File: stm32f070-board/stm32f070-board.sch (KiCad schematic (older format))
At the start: 39 parts, among them J1 USB_B_Micro, J2 USB_B_Micro, J3 Conn_01x05_Male, SW1 SW_DPDT_x2, SW2 SW_Push, SW3 SW_Push, U1 CH340G, U2 STM32F070F6P6, U3 MCP9700AT-ETT, U4 Si7055-A20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

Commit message: added mechanical drawing from ch340g soic16 and updated footprints for stm32 in schematic
Signed-off-by: suyash <in.suyash@gmail.com>
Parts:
- J3: footprint (none) -> Connector_PinHeader_1.00mm:PinHeader_1x05_P1.00mm_Vertical
- U2: footprint (none) -> stm32f070-board:TSSOP20_P0.65mm
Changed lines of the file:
@@
 F 0 "U2" H 6200 550 50  0000 C CNN
 F 1 "STM32F070F6P6" H 5850 1850 50  0000 C CNN
-F 2 "" H 5800 2000 50  0001 C CNN
+F 2 "stm32f070-board:TSSOP20_P0.65mm" H 5800 2000 50  0001 C CNN
 F 3 "http://www.farnell.com/datasheets/2281751.pdf" H 5800 2000 50  0001 C CNN
 F 4 "https://in.element14.com/stmicroelectronics/stm32f070f6p6tr/mcu-32bit-48mhz-tssop-20/dp/3129808?ost=3129808&ddkey=https%3Aen-IN%2FElement14_India%2Fsearch" H 5950 2200 50  0001 C CNN "Vendor"
@@
 F 0 "J3" H 9800 2550 50  0000 C CNN
 F 1 "Conn_01x05_Male" H 9800 2400 50  0000 C CNN
-F 2 "" H 9600 2050 50  0001 C CNN
+F 2 "Connector_PinHeader_1.00mm:PinHeader_1x05_P1.00mm_Vertical" H 9600 2050 50  0001 C CNN
 F 3 "http://www.farnell.com/datasheets/2368223.pdf" H 9600 2050 50  0001 C CNN
 F 4 "https://in.element14.com/harwin/m52-040023v0545/header-tht-vertical-1-27mm-5way/dp/1099560" H 0   0   50  0001 C CNN "Vendor"

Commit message: changed the vendor of tactile user switch from robu to element14
Signed-off-by: suyash <in.suyash@gmail.com>
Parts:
- SW2, SW3: Vendor https://robu.in/product/362-5mm-tactile-push-button-switch-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 -> https://in.element14.com/alcoswitch-te-connectivity/fsmsm/s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
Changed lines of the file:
@@
 F 1 "SW_Push" H 3850 1294 50  0000 C CNN
 F 2 "" H 3850 1300 50  0001 C CNN
-F 3 "" H 3850 1300 50  0001 C CNN
-F 4 "https://robu.in/product/362-5mm-tactile-push-button-switch-20pcs/" H 3850 1100 50  0001 C CNN "Vendor"
+F 3 "http://www.farnell.com/datasheets/1754085.pdf" H 3850 1300 50  0001 C CNN
+F 4 "https://in.element14.com/alcoswitch-te-connectivity/fsmsm/switch-spst-0-05a-24vdc-smd/dp/1703878" H 3850 1100 50  0001 C CNN "Vendor"
 	1    3850 1100
 	1    0    0    -1
@@
 F 1 "SW_Push" H 7350 1494 50  0000 C CNN
 F 2 "" H 7350 1500 50  0001 C CNN
-F 3 "" H 7350 1500 50  0001 C CNN
-F 4 "https://robu.in/product/362-5mm-tactile-push-button-switch-20pcs/" H 7350 1300 50  0001 C CNN "Vendor"
+F 3 "http://www.farnell.com/datasheets/1754085.pdf" H 7350 1500 50  0001 C CNN
+F 4 "https://in.element14.com/alcoswitch-te-connectivity/fsmsm/switch-spst-0-05a-24vdc-smd/dp/1703878" H 7350 1300 50  0001 C CNN "Vendor"
 	1    7350 1300
 	1    0    0    -1

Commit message: created footprint for tactile switch and updated it in the schematic
Signed-off-by: suyash <in.suyash@gmail.com>
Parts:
- SW2, SW3: footprint (none) -> stm32f070-board:TACTILE_SWITCH_3.5X6.0mm
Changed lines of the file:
@@
 F 0 "SW2" H 3850 1385 50  0000 C CNN
 F 1 "SW_Push" H 3850 1294 50  0000 C CNN
-F 2 "" H 3850 1300 50  0001 C CNN
+F 2 "stm32f070-board:TACTILE_SWITCH_3.5X6.0mm" H 3850 1300 50  0001 C CNN
 F 3 "http://www.farnell.com/datasheets/1754085.pdf" H 3850 1300 50  0001 C CNN
 F 4 "https://in.element14.com/alcoswitch-te-connectivity/fsmsm/switch-spst-0-05a-24vdc-smd/dp/1703878" H 3850 1100 50  0001 C CNN "Vendor"
@@
 F 0 "SW3" H 7350 1585 50  0000 C CNN
 F 1 "SW_Push" H 7350 1494 50  0000 C CNN
-F 2 "" H 7350 1500 50  0001 C CNN
+F 2 "stm32f070-board:TACTILE_SWITCH_3.5X6.0mm" H 7350 1500 50  0001 C CNN
 F 3 "http://www.farnell.com/datasheets/1754085.pdf" H 7350 1500 50  0001 C CNN
 F 4 "https://in.element14.com/alcoswitch-te-connectivity/fsmsm/switch-spst-0-05a-24vdc-smd/dp/1703878" H 7350 1300 50  0001 C CNN "Vendor"

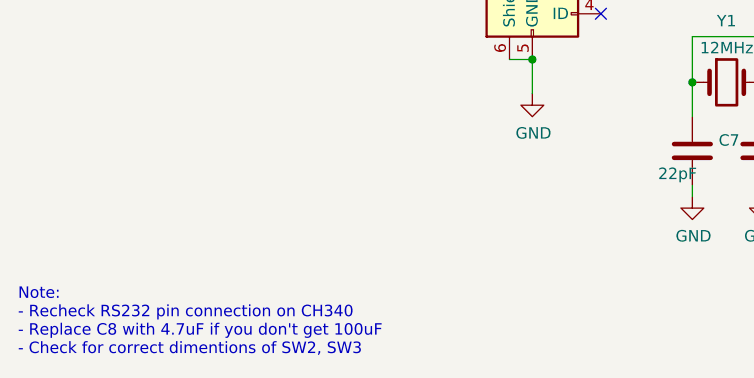
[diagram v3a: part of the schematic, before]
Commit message: created footprint for the slide switch and updated the same in schematic
Signed-off-by: suyash <in.suyash@gmail.com>
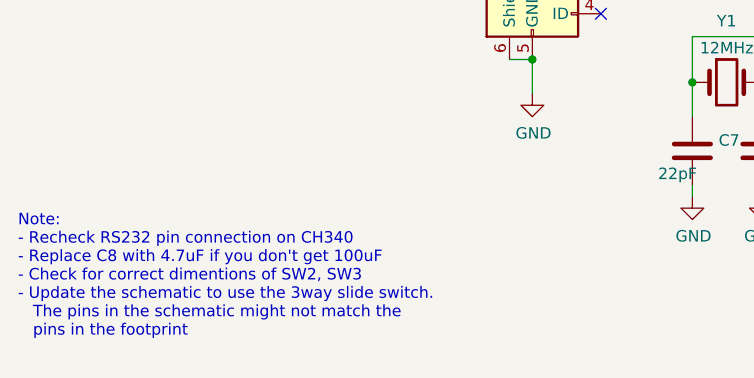
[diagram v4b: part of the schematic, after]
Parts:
- SW1: footprint (none) -> stm32f070-board:SLIDE_SWITCH_3.6x9.0mm
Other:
- note added: "Note: \n- Recheck RS232 pin connection on CH340\n- Replace C8 with 4.7uF if you don't get 100uF\n- Check for correct dimentions of SW2, SW3\n- Update the schematic to use the 3way slide switch.\n The pins in the schematic might not match the \n pins in the footprint\n\n"
- note removed: "Note: \n- Recheck RS232 pin connection on CH340\n- Replace C8 with 4.7uF if you don't get 100uF\n- Check for correct dimentions of SW2, SW3\n"
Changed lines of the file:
@@
 F 0 "SW1" H 3600 2385 50  0000 C CNN
 F 1 "SW_DPDT_x2" H 3500 2300 50  0000 C CNN
-F 2 "" H 3600 2100 50  0001 C CNN
+F 2 "stm32f070-board:SLIDE_SWITCH_3.6x9.0mm" H 3600 2100 50  0001 C CNN
 F 3 "http://www.farnell.com/datasheets/2674788.pdf" H 3600 2100 50  0001 C CNN
 F 4 "https://in.element14.com/c-k-components/js202011jcqn/slide-switch-dpdt-0-3a-6vdc-smd/dp/2931766" H 3600 2100 50  0001 C CNN "Vendor"
@@
 	7150 1300 7050 1300
 Text Notes 600  7250 0    50   ~ 0
-Note: \n- Recheck RS232 pin connection on CH340\n- Replace C8 with 4.7uF if you don't get 100uF\n- Check for correct dimentions of SW2, SW3\n
+Note: \n- Recheck RS232 pin connection on CH340\n- Replace C8 with 4.7uF if you don't get 100uF\n- Check for correct dimentions of SW2, SW3\n- Update the schematic to use the 3way slide switch.\n   The pins in the schematic might not match the \n   pins in the footprint\n\n
 Connection ~ 3800 3250
 Wire Wire Line

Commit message: added footprint for rgb led in schematic
Signed-off-by: suyash <in.suyash@gmail.com>
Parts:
- D3: footprint (none) -> stm32f070-board:PLCC6
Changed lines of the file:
@@
 F 0 "D3" H 7100 2283 50  0000 C CNN
 F 1 "LED_RGB" H 7100 2374 50  0000 C CNN
-F 2 "" H 7100 2700 50  0001 C CNN
+F 2 "stm32f070-board:PLCC6" H 7100 2700 50  0001 C CNN
 F 3 "http://www.farnell.com/datasheets/2573293.pdf" H 7100 2700 50  0001 C CNN
 F 4 "https://in.element14.com/cree/clx6f-fkc-cnp1st1e1bb7d3d3/led-aec-q101-rgb-750-1350-240mcd/dp/2840590?st=rgb%20led" H 7100 2750 50  0001 C CNN "Vendor"

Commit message: added footprint for voltage regulator and updated schematic
Signed-off-by: suyash <in.suyash@gmail.com>
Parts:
- VR1: footprint (none) -> LD39050PU33R:SON95P300X300X100-7N
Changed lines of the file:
@@
 F 0 "VR1" H 2950 3820 50  0000 C CNN
 F 1 "LD39050PU33R" H 2950 3729 50  0000 C CNN
-F 2 "" H 2950 3450 50  0001 C CNN
+F 2 "LD39050PU33R:SON95P300X300X100-7N" H 2950 3450 50  0001 C CNN
 F 3 "http://www.farnell.com/datasheets/2370074.pdf" H 2950 3450 50  0001 C CNN
 F 4 "https://in.element14.com/stmicroelectronics/ld39050pu33r/ldo-fixed-3-3v-0-5a-dfn-6/dp/2762703" H 2950 3400 50  0001 C CNN "Vendor"

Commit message: added footprint for the crystal and updated it in the schematic
Signed-off-by: suyash <in.suyash@gmail.com>
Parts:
- Y1: footprint (none) -> stm32f070-board:HC_49US-(AT49)_1
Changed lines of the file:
@@
 F 0 "Y1" H 3700 6318 50  0000 C CNN
 F 1 "12MHz" H 3700 6200 50  0000 C CNN
-F 2 "" H 3700 6050 50  0001 C CNN
+F 2 "stm32f070-board:HC_49US-(AT49)_1" H 3700 6050 50  0001 C CNN
 F 3 "http://www.farnell.com/datasheets/1883669.pdf" H 3700 6050 50  0001 C CNN
 F 4 "https://in.element14.com/abracon/abls-12-000mhz-b4-t/crystal-12mhz-18pf-hc-49us/dp/2467716" H 3700 6050 50  0001 C CNN "Vendor"

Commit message: added footprint for usb cable from mouser.in and added in schematic
Signed-off-by: suyash <in.suyash@gmail.com>
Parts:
- J1, J2: footprint (none) -> stm32f070-board:usb; Vendor https://robu.in/product/micro-usb-2-0-b-type-5-pin-connecto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 -> https://in.element14.com/molex/47346-0001/usb-conn-2-0-micr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
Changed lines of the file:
@@
 F 0 "J1" H 1355 3917 50  0000 C CNN
 F 1 "USB_B_Micro" H 1355 3826 50  0000 C CNN
-F 2 "" H 1450 3400 50  0001 C CNN
+F 2 "stm32f070-board:usb" H 1450 3400 50  0001 C CNN
 F 3 "~" H 1450 3400 50  0001 C CNN
-F 4 "https://robu.in/product/micro-usb-2-0-b-type-5-pin-connector/" H 1300 3450 50  0001 C CNN "Vendor"
+F 4 "https://in.element14.com/molex/47346-0001/usb-conn-2-0-micro-usb-type-b/dp/1568026?st=mirco%20usb%20connector" H 1300 3450 50  0001 C CNN "Vendor"
 	1    1300 3450
 	1    0    0    -1
@@
 F 0 "J2" H 2905 6017 50  0000 C CNN
 F 1 "USB_B_Micro" H 2905 5926 50  0000 C CNN
-F 2 "" H 3000 5500 50  0001 C CNN
+F 2 "stm32f070-board:usb" H 3000 5500 50  0001 C CNN
 F 3 "~" H 3000 5500 50  0001 C CNN
-F 4 "https://robu.in/product/micro-usb-2-0-b-type-5-pin-connector/" H 2850 5550 50  0001 C CNN "Vendor"
+F 4 "https://in.element14.com/molex/47346-0001/usb-conn-2-0-micro-usb-type-b/dp/1568026?st=mirco%20usb%20connector" H 2850 5550 50  0001 C CNN "Vendor"
 	1    2850 5550
 	1    0    0    -1
